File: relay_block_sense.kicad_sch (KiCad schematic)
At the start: 49 parts, among them J7 Screw_Terminal_01x02, J8 Screw_Terminal_01x10, J9 Screw_Terminal_01x10, U26 TLP3558A, U27 TLP3558A, U28 TLP3558A, U29 TLP3558A, U30 TLP3558A, U31 TLP3558A, U32 TLP3558A, U33 TLP3558A, U34 TLP3558A, U35 TLP3558A, U36 TLP3558A, U37 TLP3558A, U38 TLP3558A, U39 TLP3558A, U40 TLP3558A, U41 TLP3558A, U42 TLP3558A, U43 TLP3558A, U44 TLP3558A, U45 TLP3558A, U46 TLP3558A, U47 TLP3558A

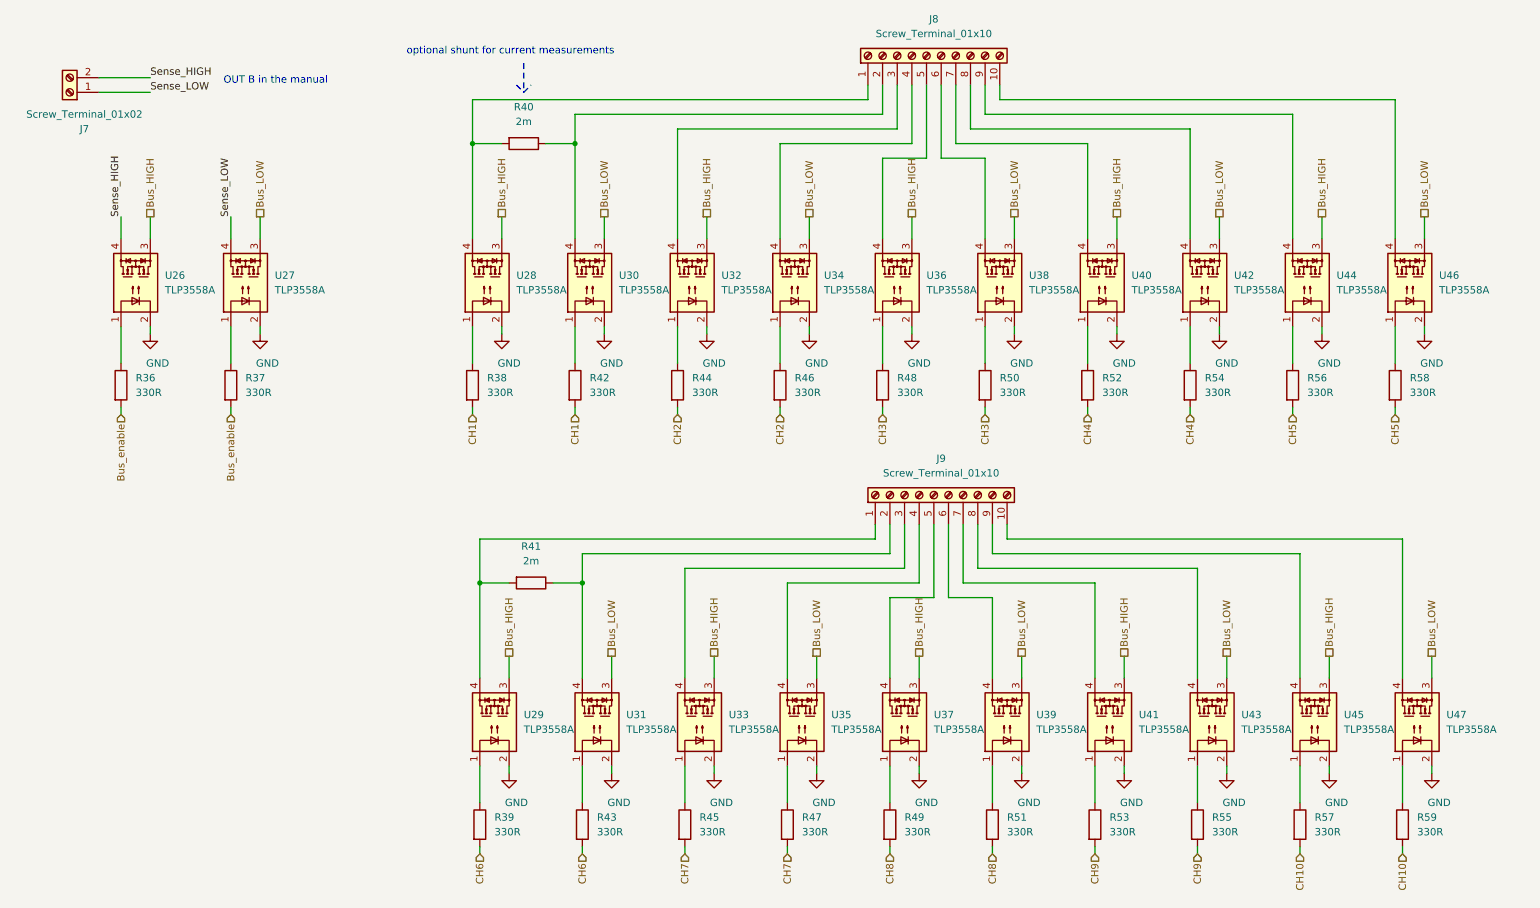
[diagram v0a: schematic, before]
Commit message: Replace the STM32 with an iCE40 FPGA (#3)
* Replaced the STM32 microcontroller with an iCE40 FPGA

* Bump version to 2.0.2, because of the update to KiCad 8

* Updated BOM properties

* Updated PCB image

* Updated readme for the FPGA version

* Updated links
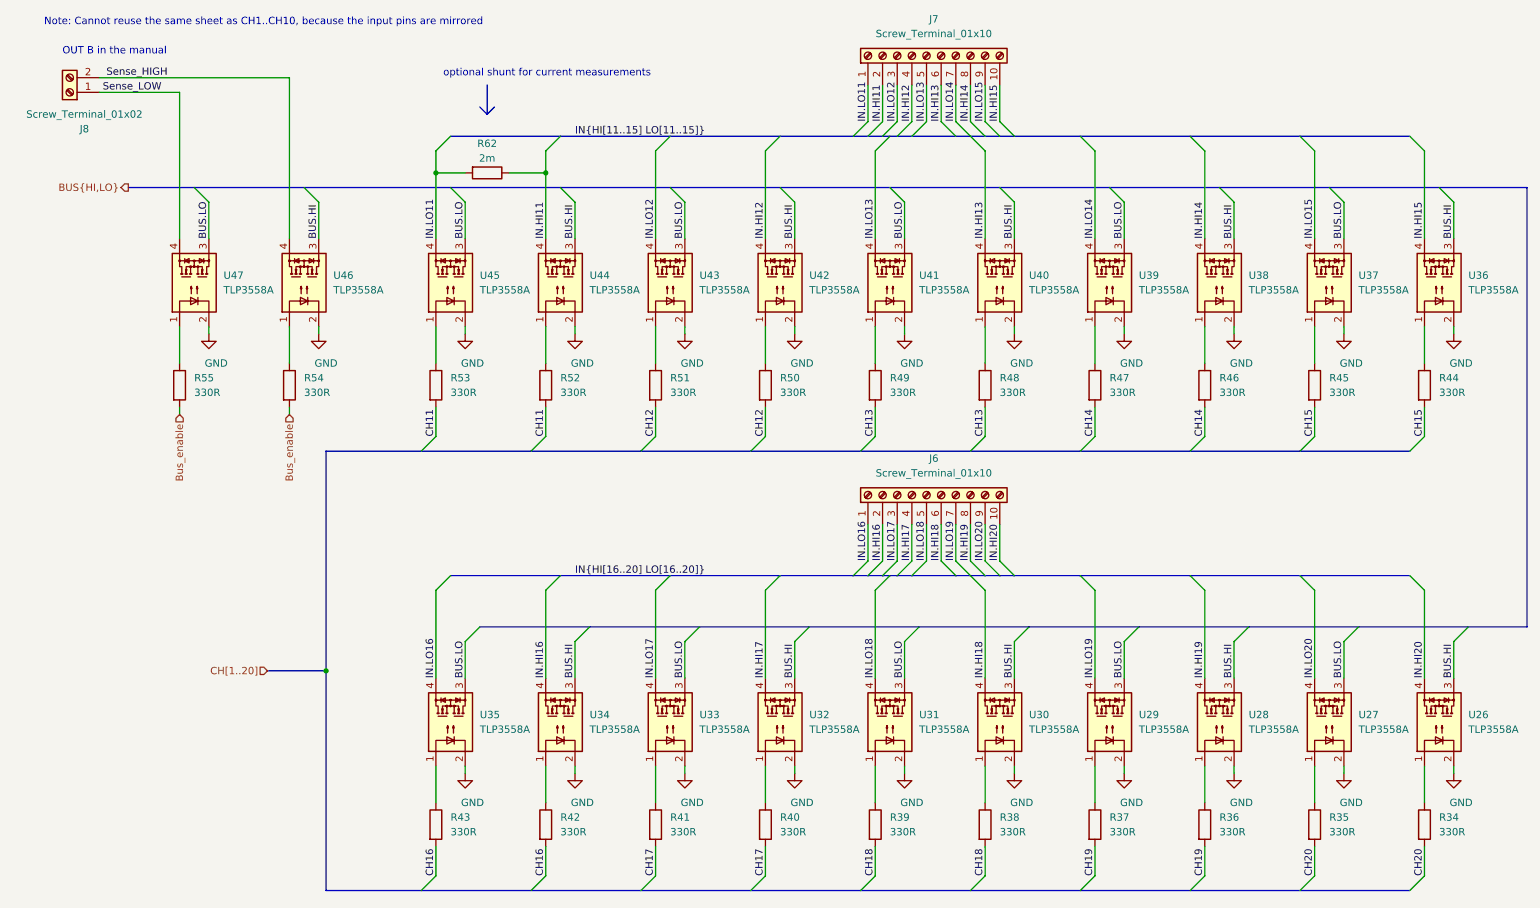
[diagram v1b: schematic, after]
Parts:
- removed R41: 2m, Resistor_SMD:R_2512_6332Metric, symbol Device:R
- J6: renamed from J9; RoHS By exemption -> Yes; Temperature Tstorage = –40 °C to 105 °C -> (none)
- J7: renamed from J8; RoHS By exemption -> Yes; Temperature Tstorage = –40 °C to 105 °C -> (none)
- J8: renamed from J7; RoHS By exemption -> Yes; Temperature Tstorage = –40 °C to 105 °C -> (none)
- R34: renamed from R59; Alternative (none) -> Yageo AC0603JR-07330RL or AC0603FR-07330RL; Note (none) -> 5% or better; PN CRCW0603330RJNEB -> CRCW0603330RJNEA
- R35: renamed from R57; Alternative (none) -> Yageo AC0603JR-07330RL or AC0603FR-07330RL; Note (none) -> 5% or better; PN CRCW0603330RJNEB -> CRCW0603330RJNEA
- R36: renamed from R55; Alternative (none) -> Yageo AC0603JR-07330RL or AC0603FR-07330RL; Note (none) -> 5% or better; PN CRCW0603330RJNEB -> CRCW0603330RJNEA
- R37: renamed from R53; Alternative (none) -> Yageo AC0603JR-07330RL or AC0603FR-07330RL; Note (none) -> 5% or better; PN CRCW0603330RJNEB -> CRCW0603330RJNEA
- R38: renamed from R51; Alternative (none) -> Yageo AC0603JR-07330RL or AC0603FR-07330RL; Note (none) -> 5% or better; PN CRCW0603330RJNEB -> CRCW0603330RJNEA
- R39: renamed from R49; Alternative (none) -> Yageo AC0603JR-07330RL or AC0603FR-07330RL; Note (none) -> 5% or better; PN CRCW0603330RJNEB -> CRCW0603330RJNEA
- R40: renamed from R47; Alternative (none) -> Yageo AC0603JR-07330RL or AC0603FR-07330RL; Note (none) -> 5% or better; PN CRCW0603330RJNEB -> CRCW0603330RJNEA
- R41: renamed from R45; Alternative (none) -> Yageo AC0603JR-07330RL or AC0603FR-07330RL; Note (none) -> 5% or better; PN CRCW0603330RJNEB -> CRCW0603330RJNEA
- R42: renamed from R43; Alternative (none) -> Yageo AC0603JR-07330RL or AC0603FR-07330RL; Note (none) -> 5% or better; PN CRCW0603330RJNEB -> CRCW0603330RJNEA
- R43: renamed from R39; Alternative (none) -> Yageo AC0603JR-07330RL or AC0603FR-07330RL; Note (none) -> 5% or better; PN CRCW0603330RJNEB -> CRCW0603330RJNEA
- R44: renamed from R58; Alternative (none) -> Yageo AC0603JR-07330RL or AC0603FR-07330RL; Note (none) -> 5% or better; PN CRCW0603330RJNEB -> CRCW0603330RJNEA
- R45: renamed from R56; Alternative (none) -> Yageo AC0603JR-07330RL or AC0603FR-07330RL; Note (none) -> 5% or better; PN CRCW0603330RJNEB -> CRCW0603330RJNEA
- R46: renamed from R54; Alternative (none) -> Yageo AC0603JR-07330RL or AC0603FR-07330RL; Note (none) -> 5% or better; PN CRCW0603330RJNEB -> CRCW0603330RJNEA
- R47: renamed from R52; Alternative (none) -> Yageo AC0603JR-07330RL or AC0603FR-07330RL; Note (none) -> 5% or better; PN CRCW0603330RJNEB -> CRCW0603330RJNEA
- R48: renamed from R50; Alternative (none) -> Yageo AC0603JR-07330RL or AC0603FR-07330RL; Note (none) -> 5% or better; PN CRCW0603330RJNEB -> CRCW0603330RJNEA
- R49: renamed from R48; Alternative (none) -> Yageo AC0603JR-07330RL or AC0603FR-07330RL; Note (none) -> 5% or better; PN CRCW0603330RJNEB -> CRCW0603330RJNEA
- R50: renamed from R46; Alternative (none) -> Yageo AC0603JR-07330RL or AC0603FR-07330RL; Note (none) -> 5% or better; PN CRCW0603330RJNEB -> CRCW0603330RJNEA
- R51: renamed from R44; Alternative (none) -> Yageo AC0603JR-07330RL or AC0603FR-07330RL; Note (none) -> 5% or better; PN CRCW0603330RJNEB -> CRCW0603330RJNEA
- R52: renamed from R42; Alternative (none) -> Yageo AC0603JR-07330RL or AC0603FR-07330RL; Note (none) -> 5% or better; PN CRCW0603330RJNEB -> CRCW0603330RJNEA
- R53: renamed from R38; Alternative (none) -> Yageo AC0603JR-07330RL or AC0603FR-07330RL; Note (none) -> 5% or better; PN CRCW0603330RJNEB -> CRCW0603330RJNEA
- R54: renamed from R36; Alternative (none) -> Yageo AC0603JR-07330RL or AC0603FR-07330RL; Note (none) -> 5% or better; PN CRCW0603330RJNEB -> CRCW0603330RJNEA
- R55: renamed from R37; Alternative (none) -> Yageo AC0603JR-07330RL or AC0603FR-07330RL; Note (none) -> 5% or better; PN CRCW0603330RJNEB -> CRCW0603330RJNEA
- R62: renamed from R40; Config (none) -> do not fit
- renumbered U47 to U26, U45 to U27, U43 to U28, U41 to U29, U39 to U30, U37 to U31, U35 to U32, U31 to U34, U29 to U35, U46 to U36, U44 to U37, U42 to U38, U40 to U39, U38 to U40, U36 to U41, U34 to U42, U32 to U43, U30 to U44, U28 to U45, U26 to U46, U27 to U47
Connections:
- net IN.HI12: now reaches J7.4 (Pin_4), U42.4
- net IN.LO13: now reaches J7.5 (Pin_5), U41.4
- net IN.HI13: now reaches J7.6 (Pin_6), U40.4
- net IN.HI14: now reaches J7.8 (Pin_8), U38.4
- net IN.HI16: now reaches J6.2 (Pin_2), U34.4
- net IN.LO18: now reaches J6.5 (Pin_5), U31.4
- net IN.HI19: now reaches J6.8 (Pin_8), U28.4
- net IN.HI11: now reaches J7.2 (Pin_2), R62.1, U44.4
- net IN.LO11: now reaches J7.1 (Pin_1), R62.2, U45.4
- net IN.LO16: now reaches J6.1 (Pin_1), U35.4
- net IN.HI15: now reaches J7.10 (Pin_10), U36.4
- net IN.LO12: now reaches J7.3 (Pin_3), U43.4
- net IN.LO14: now reaches J7.7 (Pin_7), U39.4
- net IN.LO15: now reaches J7.9 (Pin_9), U37.4
- net IN.HI20: now reaches J6.10 (Pin_10), U26.4
- net IN.LO17: now reaches J6.3 (Pin_3), U33.4
- net IN.HI17: now reaches J6.4 (Pin_4), U32.4
- net IN.HI18: now reaches J6.6 (Pin_6), U30.4
- net IN.LO19: now reaches J6.7 (Pin_7), U29.4
- net IN.LO20: now reaches J6.9 (Pin_9), U27.4
- net Bus_HIGH renamed BUS.LO
- net BUS.LO: now also U47.3; no longer U46.3
- net Bus_LOW renamed BUS.HI
- net BUS.HI: now also U46.3; no longer U47.3
- net CH1 renamed CH11
- net CH10 renamed CH20
- net CH2 renamed CH12
- net CH3 renamed CH13
- net CH4 renamed CH14
- net CH5 renamed CH15
- net CH6 renamed CH16
- net CH7 renamed CH17
- net CH8 renamed CH18
- net CH9 renamed CH19
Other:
- note added: "Note: Cannot reuse the same sheet as CH1..CH10, because the input pins are mirrored"
- moved on the sheet: J6, R34, R35, R36, R38, R39, R40, R41, R42, R43, R44, R45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
